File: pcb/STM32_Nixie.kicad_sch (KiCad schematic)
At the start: 0 parts

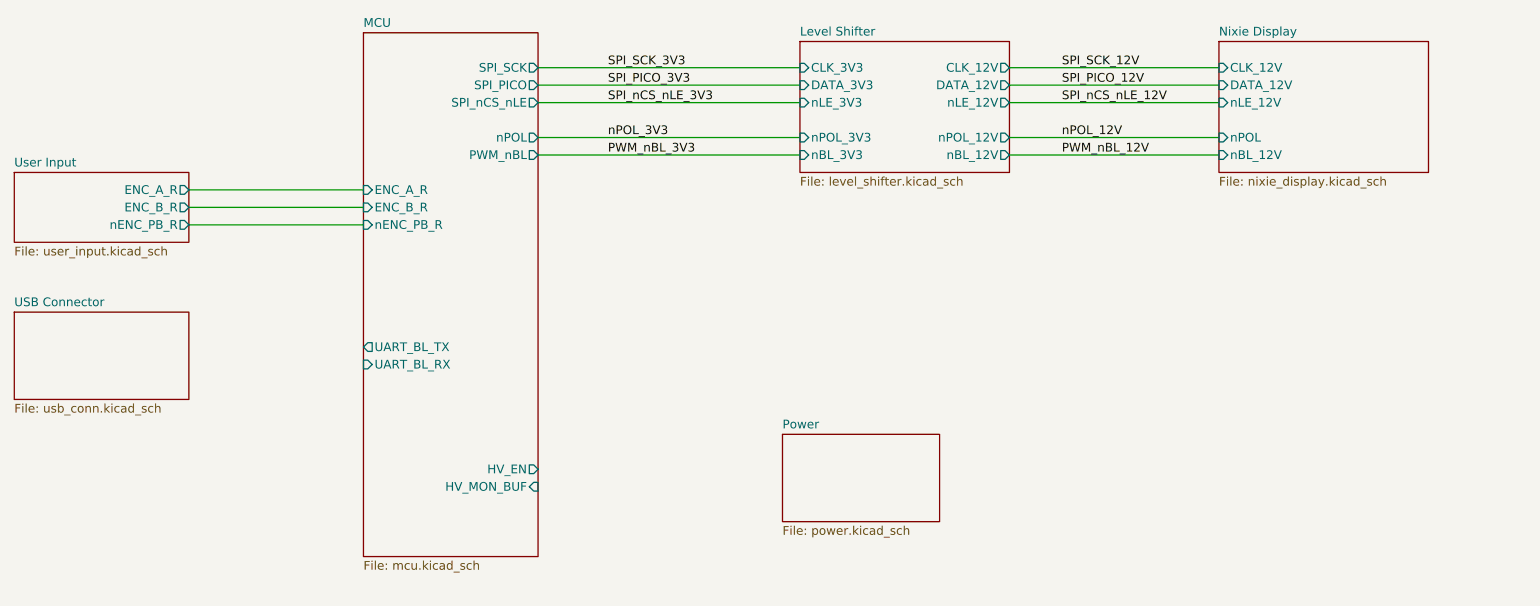
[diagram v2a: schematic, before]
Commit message: Added 12V and 180V sense lines
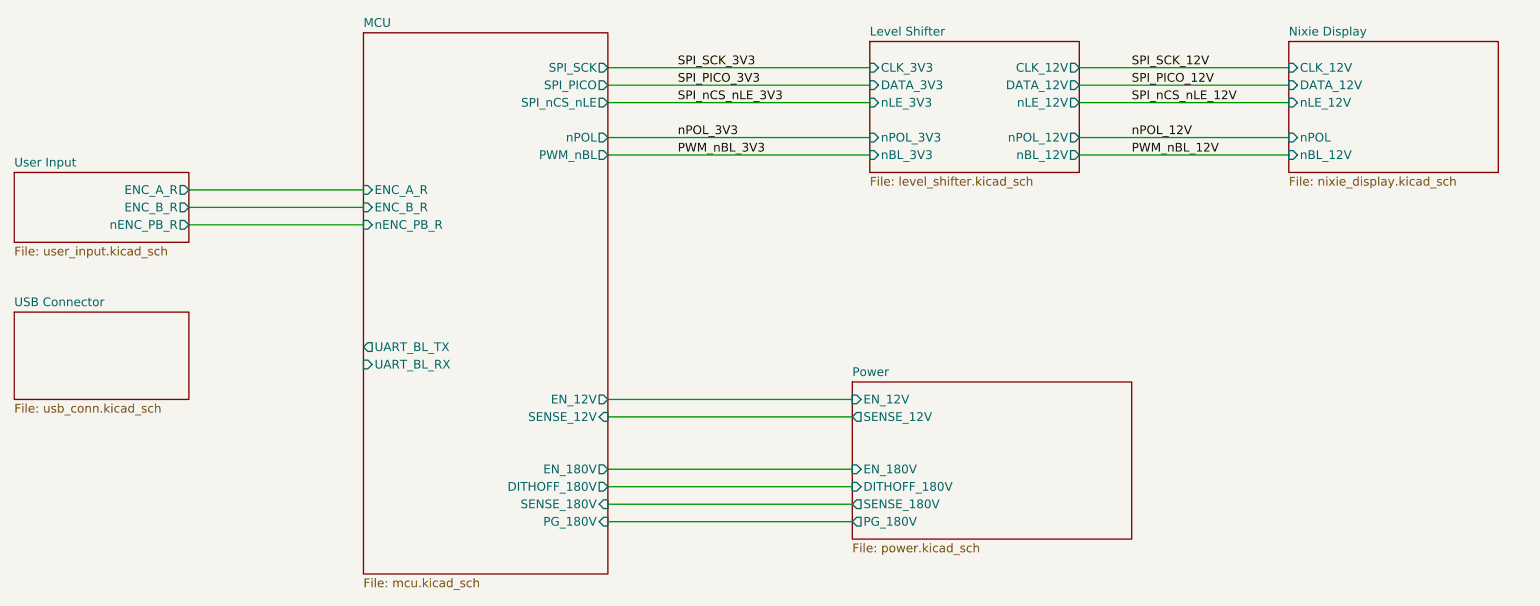
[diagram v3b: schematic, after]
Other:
- sheet MCU ports: added DITHOFF_180V, EN_12V, EN_180V, PG_180V, SENSE_12V, SENSE_180V; removed HV_EN, HV_MON_BUF
- sheet Power ports: added DITHOFF_180V, EN_12V, EN_180V, PG_180V, SENSE_12V, SENSE_180V; removed none

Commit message: Updated ftdi page
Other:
- title: (none) -> STM32 Nixie Clock
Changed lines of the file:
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@@
 (kicad_sch (version 20211123) (generator eeschema)
   (paper "A4")
+  (title_block
+    (title "STM32 Nixie Clock")
+    (date "2024-05-14")
+    (rev "1")
+  )
   (wire (pts (xy 190.5 68.58) (xy 220.98 68.58))
     (stroke (width 0) (type default) (color 0 0 0 0))
@@
     )
   )
-  (sheet (at 157.48 109.22) (size 40.64 22.86) (fields_autoplaced)
+  (sheet (at 157.48 109.22) (size 22.86 22.86) (fields_autoplaced)
     (stroke (width 0.1524) (type solid) (color 0 0 0 0))
     (fill (color 0 0 0 0.0000))
@@
       (reference "#PWR088") (unit 1) (value "GND") (footprint "")
     )
+    (path "/c489a08b-e150-4d56-8df0-484cd36f24a0/3a0a3a05-0c70-4fa1-ba5b-b357b288f85f"
+      (reference "#PWR?") (unit 1) (value "GND") (footprint "")
+    )
+    (path "/c489a08b-e150-4d56-8df0-484cd36f24a0/3e780543-9bd0-4171-9337-1950d8523fdd"
+      (reference "#PWR?") (unit 1) (value "GND") (footprint "")
+    )
+    (path "/c489a08b-e150-4d56-8df0-484cd36f24a0/4b52de59-6014-453b-88ae-8f5c598c97cb"
+      (reference "#PWR?") (unit 1) (value "GND") (footprint "")
+    )
+    (path "/c489a08b-e150-4d56-8df0-484cd36f24a0/57811ecc-5d57-4b17-bd64-2db53629c2be"
+      (reference "#PWR?") (unit 1) (value "GND") (footprint "")
+    )
+    (path "/c489a08b-e150-4d56-8df0-484cd36f24a0/6e3cb90a-f92b-439f-a7fe-b190dc399ecd"
+      (reference "#PWR?") (unit 1) (value "GND") (footprint "")
+    )
+    (path "/c489a08b-e150-4d56-8df0-484cd36f24a0/c690e4ec-3984-4937-8db3-234b2e14834a"
+      (reference "#PWR?") (unit 1) (value "+3.3V") (footprint "")
+    )
+    (path "/c489a08b-e150-4d56-8df0-484cd36f24a0/d04cee2e-f8eb-4148-b846-9062ce6eff47"
+      (reference "#PWR?") (unit 1) (value "+3.3V") (footprint "")
+    )
+    (path "/c489a08b-e150-4d56-8df0-484cd36f24a0/d5d9fe9c-b5ab-40bb-83ae-13f558f7dfb0"
+      (reference "#PWR?") (unit 1) (value "+3.3V") (footprint "")
+    )
+    (path "/c489a08b-e150-4d56-8df0-484cd36f24a0/e50ccdcd-5ba3-467d-beb6-27ecff2709d1"
+      (reference "#PWR?") (unit 1) (value "GND") (footprint "")
+    )
+    (path "/c489a08b-e150-4d56-8df0-484cd36f24a0/f7111125-1cb4-42fa-ba48-74acf8a6cb33"
+      (reference "#PWR?") (unit 1) (value "+3.3V") (footprint "")
+    )
+    (path "/c489a08b-e150-4d56-8df0-484cd36f24a0/f7d5b02e-1301-403e-a01e-6af08cd5cec8"
+      (reference "#PWR?") (unit 1) (value "+3.3V") (footprint "")
+    )
     (path "/8ecdbb98-5b2a-4725-a227-62b58d0c66f3/82d4e7bc-49e8-418b-8c34-f46f3717b905"
       (reference "BAT1") (unit 1) (value "BS-7") (footprint "arjun_footprints:Battery_Holder_Coin_2032_BS-7")
@@
       (reference "C55") (unit 1) (value "CAP_CER_0u1_50V_X7R_0603") (footprint "Capacitor_SMD:C_0603_1608Metric")
     )
+    (path "/c489a08b-e150-4d56-8df0-484cd36f24a0/5783e9cc-debe-47cd-8aa6-59e6d896548c"
+      (reference "C?") (unit 1) (value "CAP_CER_47p_50V_NP0_0603") (footprint "Capacitor_SMD:C_0603_1608Metric")
+    )
+    (path "/c489a08b-e150-4d56-8df0-484cd36f24a0/78de814c-81ac-4993-a07e-fc5048c1a781"
+      (reference "C?") (unit 1) (value "CAP_CER_4u7_16V_X7R_0805") (footprint "Capacitor_SMD:C_0805_2012Metric")
+    )
+    (path "/c489a08b-e150-4d56-8df0-484cd36f24a0/953aa900-78d2-42b5-8998-ed6ad5097287"
+      (reference "C?") (unit 1) (value "CAP_CER_0u1_50V_X7R_0603") (footprint "Capacitor_SMD:C_0603_1608Metric")
+    )
+    (path "/c489a08b-e150-4d56-8df0-484cd36f24a0/99e2d617-fd0c-4b29-ab39-abc6222e8341"
+      (reference "C?") (unit 1) (value "CAP_CER_0u1_50V_X7R_0603") (footprint "Capacitor_SMD:C_0603_1608Metric")
+    )
+    (path "/c489a08b-e150-4d56-8df0-484cd36f24a0/ba49ad5e-e30b-423a-954d-b6d003ea5f2c"
+      (reference "C?") (unit 1) (value "CAP_CER_0u1_50V_X7R_0603") (footprint "Capacitor_SMD:C_0603_1608Metric")
+    )
+    (path "/c489a08b-e150-4d56-8df0-484cd36f24a0/e3d62874-90a1-46c9-8f32-f846c6e2456c"
+      (reference "C?") (unit 1) (value "CAP_CER_47p_50V_NP0_0603") (footprint "Capacitor_SMD:C_0603_1608Metric")
+    )
+    (path "/c489a08b-e150-4d56-8df0-484cd36f24a0/f3e5509a-449b-4dbe-a8b8-78989b76835d"
+      (reference "C?") (unit 1) (value "CAP_CER_0u1_50V_X7R_0603") (footprint "Capacitor_SMD:C_0603_1608Metric")
+    )
     (path "/b6f49995-0eb9-4525-a397-4f1a1965a188/6f254da5-1c00-4a7b-a68b-a745bcbb22c0"
       (reference "D1") (unit 1) (value "D_300V_2A_SMB") (footprint "Diode_SMD:D_SMB")
     )
+    (path "/c489a08b-e150-4d56-8df0-484cd36f24a0/11a01d7c-03f4-4357-abd3-08189dc2e83b"
+      (reference "D?") (unit 1) (value "LED_GREEN_0603") (footprint "LED_SMD:LED_0603_1608Metric")
+    )
+    (path "/c489a08b-e150-4d56-8df0-484cd36f24a0/910eee7a-45f3-47c2-87b2-570024195aee"
+      (reference "D?") (unit 1) (value "LED_AMBER_0603") (footprint "LED_SMD:LED_0603_1608Metric")
+    )
     (path "/8ecdbb98-5b2a-4725-a227-62b58d0c66f3/9ff1a288-eeb2-4e85-b12c-ae7a5d737238"
       (reference "FB1") (unit 1) (value "FER_1K_0A6_0603") (footprint "Inductor_SMD:L_0603_1608Metric")
@@
       (reference "R46") (unit 1) (value "RES_4K7_1P_1/10W_0603") (footprint "Resistor_SMD:R_0603_1608Metric")
     )
+    (path "/c489a08b-e150-4d56-8df0-484cd36f24a0/0024d9b4-31d7-40b8-b1d6-1e8039817e5e"
+      (reference "R?") (unit 1) (value "RES_27R_1P_1/10W_0603") (footprint "Resistor_SMD:R_0603_1608Metric")
+    )
+    (path "/c489a08b-e150-4d56-8df0-484cd36f24a0/178a63ec-7915-46d0-a26d-9ff3ccd9c6f2"
+      (reference "R?") (unit 1) (value "RES_698R_1P_1/10W_0603") (footprint "Resistor_SMD:R_0603_1608Metric")
+    )
+    (path "/c489a08b-e150-4d56-8df0-484cd36f24a0/292ab537-63d1-4bac-aa17-ef0b79442798"
+      (reference "R?") (unit 1) (value "RES_27R_1P_1/10W_0603") (footprint "Resistor_SMD:R_0603_1608Metric")
+    )
+    (path "/c489a08b-e150-4d56-8df0-484cd36f24a0/b25a3974-ac48-4a45-aaab-fe910f8c2fdb"
+      (reference "R?") (unit 1) (value "RES_10K_1P_1/10W_0603") (footprint "Resistor_SMD:R_0603_1608Metric")
+    )
+    (path "/c489a08b-e150-4d56-8df0-484cd36f24a0/c207a93b-ecd4-4d99-8cda-c931ae53446f"
+      (reference "R?") (unit 1) (value "RES_1K5_1P_1/10W_0603") (footprint "Resistor_SMD:R_0603_1608Metric")
+    )
     (path "/8ecdbb98-5b2a-4725-a227-62b58d0c66f3/f07b1648-daa4-4991-bc04-ece7d3c88607"

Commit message: Added load swtich current limit change FET and plumbed out signals to top level
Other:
- sheet USB Connector ports: added SET_ILIM, UART_BL_RX, UART_BL_TX; removed none
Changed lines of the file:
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@@
+    (stroke (width 0) (type default) (color 0 0 0 0))
+  )
+  (wire (pts (xy 60.96 106.68) (xy 86.36 106.68))
     (stroke (width 0) (type default) (color 0 0 0 0))
   )
@@
   )
   (wire (pts (xy 121.92 127) (xy 157.48 127))
+    (stroke (width 0) (type default) (color 0 0 0 0))
+  )
+  (wire (pts (xy 60.96 104.14) (xy 86.36 104.14))
     (stroke (width 0) (type default) (color 0 0 0 0))
   )
@@
     )
   )
-  (sheet (at 35.56 99.06) (size 25.4 12.7) (fields_autoplaced)
+  (sheet (at 35.56 99.06) (size 25.4 17.78) (fields_autoplaced)
     (stroke (width 0.1524) (type solid) (color 0 0 0 0))
     (fill (color 0 0 0 0.0000))
@@
       (effects (font (size 1.27 1.27)) (justify left bottom))
     )
-    (property "Sheet file" "usb_conn.kicad_sch" (id 1) (at 35.56 112.3446 0)
+    (property "Sheet file" "usb_conn.kicad_sch" (id 1) (at 35.56 117.4246 0)
       (effects (font (size 1.27 1.27)) (justify left top))
+    )
+    (pin "UART_BL_TX" input (at 60.96 104.14 0)
+      (effects (font (size 1.27 1.27)) (justify right))
+    )
+    (pin "UART_BL_RX" output (at 60.96 106.68 0)
+      (effects (font (size 1.27 1.27)) (justify right))
+    )
+    (pin "SET_ILIM" input (at 60.96 111.76 0)
+      (effects (font (size 1.27 1.27)) (justify right))
     )
   )
@@
       (reference "R55") (unit 1) (value "RES_26K1_1P_1/10W_0603") (footprint "Resistor_SMD:R_0603_1608Metric")
     )
+    (path "/c489a08b-e150-4d56-8df0-484cd36f24a0/84b8d0c6-3431-4d2c-ace9-2165e82bcc93"
+      (reference "R56") (unit 1) (value "RES_10K_1P_1/10W_0603") (footprint "Resistor_SMD:R_0603_1608Metric")
+    )
     (path "/8ecdbb98-5b2a-4725-a227-62b58d0c66f3/f07b1648-daa4-4991-bc04-ece7d3c88607"

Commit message: Added ESD protection to 5V input, leds, hw rev pins, and test points.
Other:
- sheet MCU ports: added SET_ILIM; removed none
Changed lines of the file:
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@@
+    (stroke (width 0) (type default) (color 0 0 0 0))
+  )
+  (wire (pts (xy 60.96 111.76) (xy 86.36 111.76))
     (stroke (width 0) (type default) (color 0 0 0 0))
   )
@@
     (pin "EN_12V" output (at 121.92 111.76 0)
       (effects (font (size 1.27 1.27)) (justify right))
+    )
+    (pin "SET_ILIM" output (at 86.36 111.76 180)
+      (effects (font (size 1.27 1.27)) (justify left))
     )
   )
@@
       (reference "#PWR0103") (unit 1) (value "GND") (footprint "")
     )
+    (path "/c489a08b-e150-4d56-8df0-484cd36f24a0/d08d2167-b791-4683-b0fd-d03bde8a9858"
+      (reference "#PWR0104") (unit 1) (value "GND") (footprint "")
+    )
+    (path "/c489a08b-e150-4d56-8df0-484cd36f24a0/f17c634e-1941-43fc-ad44-0304d2911ddc"
+      (reference "#PWR0105") (unit 1) (value "GND") (footprint "")
+    )
+    (path "/8ecdbb98-5b2a-4725-a227-62b58d0c66f3/5167f26f-8bd8-40cb-a2a9-9eb859561930"
+      (reference "#PWR0106") (unit 1) (value "+3.3V") (footprint "")
+    )
+    (path "/8ecdbb98-5b2a-4725-a227-62b58d0c66f3/2a6342c1-4525-472b-8934-9ca1edf0d110"
+      (reference "#PWR0107") (unit 1) (value "GND") (footprint "")
+    )
+    (path "/b6f49995-0eb9-4525-a397-4f1a1965a188/673ccf88-29e0-49f5-a587-5fce5969abb4"
+      (reference "#PWR0108") (unit 1) (value "GND") (footprint "")
+    )
+    (path "/b6f49995-0eb9-4525-a397-4f1a1965a188/cf229b73-06b4-4463-bb82-69f08158c973"
+      (reference "#PWR0109") (unit 1) (value "+12V") (footprint "")
+    )
+    (path "/b6f49995-0eb9-4525-a397-4f1a1965a188/d1500df6-5983-41ae-8ef7-821da9630241"
+      (reference "#PWR0110") (unit 1) (value "GND") (footprint "")
+    )
+    (path "/b6f49995-0eb9-4525-a397-4f1a1965a188/a8fb0327-0ea9-4995-8b63-1a91c6865ca3"
+      (reference "#PWR0111") (unit 1) (value "+3.3V") (footprint "")
+    )
+    (path "/b6f49995-0eb9-4525-a397-4f1a1965a188/ad606118-c669-4fb2-99fb-41c5e012ca1e"
+      (reference "#PWR0112") (unit 1) (value "GND") (footprint "")
+    )
     (path "/8ecdbb98-5b2a-4725-a227-62b58d0c66f3/82d4e7bc-49e8-418b-8c34-f46f3717b905"
       (reference "BAT1") (unit 1) (value "BS-7") (footprint "arjun_footprints:Battery_Holder_Coin_2032_BS-7")
@@
       (reference "D3") (unit 1) (value "LED_GREEN_0603") (footprint "LED_SMD:LED_0603_1608Metric")
     )
+    (path "/c489a08b-e150-4d56-8df0-484cd36f24a0/ee94a7e4-ba9a-4e33-8d5a-6abdcc7761d9"
+      (reference "D4") (unit 1) (value "D_TVS_BI_3V6_20W_3-XFDFN") (footprint "arjun_footprints:DIO_ESD122DMYR")
+    )
     (path "/c489a08b-e150-4d56-8df0-484cd36f24a0/439969e1-6954-4451-9e37-a46ae6e0fb7b"
-      (reference "D?") (unit 1) (value "LED_RED_0603") (footprint "LED_SMD:LED_0603_1608Metric")
+      (reference "D5") (unit 1) (value "LED_RED_0603") (footprint "LED_SMD:LED_0603_1608Metric")
+    )
+    (path "/c489a08b-e150-4d56-8df0-484cd36f24a0/51d99345-ea33-401b-87b5-9e04fea58100"
+      (reference "D6") (unit 1) (value "D_TVS_UNI_5V_700W_2-UDFN") (footprint "arjun_footprints:QFN-2L_STM")
+    )
+    (path "/8ecdbb98-5b2a-4725-a227-62b58d0c66f3/44d0a881-4349-41e6-b0de-4b62c2fab965"
+      (reference "D7") (unit 1) (value "LED_RGB_0606") (footprint "arjun_footprints:EAST1616RGBB2_EVE")
+    )
+    (path "/b6f49995-0eb9-4525-a397-4f1a1965a188/bef418bc-c2a6-4582-89cb-80573aa218fc"
+      (reference "D8") (unit 1) (value "LED_AMBER_0603") (footprint "LED_SMD:LED_0603_1608Metric")
+    )
+    (path "/b6f49995-0eb9-4525-a397-4f1a1965a188/357ae48b-cb82-42ff-89e5-d5b92590cdea"
+      (reference "D9") (unit 1) (value "LED_GREEN_0603") (footprint "LED_SMD:LED_0603_1608Metric")
+    )
+    (path "/b6f49995-0eb9-4525-a397-4f1a1965a188/f6f5e26b-758d-4868-a9cf-710aa27c872a"
+      (reference "D10") (unit 1) (value "LED_GREEN_0603") (footprint "LED_SMD:LED_0603_1608Metric")
     )
     (path "/8ecdbb98-5b2a-4725-a227-62b58d0c66f3/9ff1a288-eeb2-4e85-b12c-ae7a5d737238"
@@
     )
     (path "/c489a08b-e150-4d56-8df0-484cd36f24a0/63f1e869-10e5-4eef-91d8-56741cdaef9c"
-      (reference "R?") (unit 1) (value "RES_3K3_1P_1/10W_0603") (footprint "Resistor_SMD:R_0603_1608Metric")
+      (reference "R57") (unit 1) (value "RES_3K3_1P_1/10W_0603") (footprint "Resistor_SMD:R_0603_1608Metric")
+    )
+    (path "/8ecdbb98-5b2a-4725-a227-62b58d0c66f3/264b9174-9fc9-4a3c-8317-d3c783cf6260"
+      (reference "R58") (unit 1) (value "RES_499R_1P_1/10W_0603") (footprint "Resistor_SMD:R_0603_1608Metric")
+    )
+    (path "/8ecdbb98-5b2a-4725-a227-62b58d0c66f3/a7482b2b-e350-4873-b2e0-d0f133abf36b"
+      (reference "R59") (unit 1) (value "RES_1K5_1P_1/10W_0603") (footprint "Resistor_SMD:R_0603_1608Metric")
+    )
+    (path "/8ecdbb98-5b2a-4725-a227-62b58d0c66f3/4143ced6-45e0-4620-957a-8e689e753100"
+      (reference "R60") (unit 1) (value "RES_698R_1P_1/10W_0603") (footprint "Resistor_SMD:R_0603_1608Metric")
+    )
+    (path "/8ecdbb98-5b2a-4725-a227-62b58d0c66f3/80b08d81-5224-4f77-abc5-72641d7143c5"
+      (reference "R61") (unit 1) (value "RES_10K_1P_1/10W_0603") (footprint "Resistor_SMD:R_0603_1608Metric")
+    )
+    (path "/8ecdbb98-5b2a-4725-a227-62b58d0c66f3/96ea68b7-450d-468d-a7a5-cd755652b739"
+      (reference "R62") (unit 1) (value "RES_10K_1P_1/10W_0603") (footprint "Resistor_SMD:R_0603_1608Metric")
+    )
+    (path "/8ecdbb98-5b2a-4725-a227-62b58d0c66f3/e61198c1-11dd-49e2-8e5a-dc81547c6429"
+      (reference "R63") (unit 1) (value "RES_10K_1P_1/10W_0603") (footprint "Resistor_SMD:R_0603_1608Metric")
+    )
+    (path "/8ecdbb98-5b2a-4725-a227-62b58d0c66f3/4b13dffe-fae6-4a07-ba8e-da8dd3733948"
+      (reference "R64") (unit 1) (value "RES_30R_1P_1/10W_0603") (footprint "Resistor_SMD:R_0603_1608Metric")
+    )
+    (path "/8ecdbb98-5b2a-4725-a227-62b58d0c66f3/704a5148-048e-44d6-93b1-5dd975decc20"
+      (reference "R65") (unit 1) (value "RES_30R_1P_1/10W_0603") (footprint "Resistor_SMD:R_0603_1608Metric")
+    )
+    (path "/8ecdbb98-5b2a-4725-a227-62b58d0c66f3/852cf1dd-b67f-4720-b5d8-7007dfa1d840"
+      (reference "R66") (unit 1) (value "RES_30R_1P_1/10W_0603") (footprint "Resistor_SMD:R_0603_1608Metric")
+    )
+    (path "/b6f49995-0eb9-4525-a397-4f1a1965a188/ca0ad8e0-dc51-464e-8f15-7bfae6ebbfae"
+      (reference "R67") (unit 1) (value "RES_1K5_1P_1/10W_0603") (footprint "Resistor_SMD:R_0603_1608Metric")
+    )
+    (path "/b6f49995-0eb9-4525-a397-4f1a1965a188/719057d6-24fc-4db5-bef4-5588a9e33ec2"
+      (reference "R68") (unit 1) (value "RES_9K31_1P_1/10W_0603") (footprint "Resistor_SMD:R_0603_1608Metric")
+    )
+    (path "/b6f49995-0eb9-4525-a397-4f1a1965a188/0b71bd87-fde8-4fbe-b3e7-778ee361b7ac"
+      (reference "R69") (unit 1) (value "RES_698R_1P_1/10W_0603") (footprint "Resistor_SMD:R_0603_1608Metric")
     )
     (path "/8ecdbb98-5b2a-4725-a227-62b58d0c66f3/f07b1648-daa4-4991-bc04-ece7d3c88607"
@@
       (reference "TP1") (unit 1) (value "RTC_OUT") (footprint "arjun_footprints:TestPoint_Keystone_5019_Minature")
     )
+    (path "/b6f49995-0eb9-4525-a397-4f1a1965a188/0e188862-ba49-4e89-ba27-975eba221aa3"
+      (reference "TP?") (unit 1) (value "TP_KEYSTONE_5019") (footprint "arjun_footprints:TestPoint_Keystone_5019_Minature")
+    )
+    (path "/c489a08b-e150-4d56-8df0-484cd36f24a0/17dc6b5c-1c2a-4b19-8f56-2fdfff259811"
+      (reference "TP?") (unit 1) (value "TP_KEYSTONE_5019") (footprint "arjun_footprints:TestPoint_Keystone_5019_Minature")
+    )
+    (path "/c489a08b-e150-4d56-8df0-484cd36f24a0/6930bbd7-b962-4070-9b46-800d9508ad1e"
+      (reference "TP?") (unit 1) (value "TP_KEYSTONE_5019") (footprint "arjun_footprints:TestPoint_Keystone_5019_Minature")
+    )
+    (path "/b6f49995-0eb9-4525-a397-4f1a1965a188/6e96e4c2-209a-4f7f-98c6-4e4ce8d2f994"
+      (reference "TP?") (unit 1) (value "TP_KEYSTONE_5019") (footprint "arjun_footprints:TestPoint_Keystone_5019_Minature")
+    )
+    (path "/b6f49995-0eb9-4525-a397-4f1a1965a188/b9c3691b-e2ac-490a-a376-134a6b3b9ca6"
+      (reference "TP?") (unit 1) (value "TP_KEYSTONE_5019") (footprint "arjun_footprints:TestPoint_Keystone_5019_Minature")
+    )
     (path "/f14ed119-44a4-4dba-a5a7-78813bb44ce1/cd04ffbb-d169-4465-9b0c-c22c39907f5b"
